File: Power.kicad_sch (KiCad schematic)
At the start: 21 parts, among them U1 HT75xx-1-SOT89, U2 TLV62569DBV, U3 MCP6001-OT

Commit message: Adding official files from course download
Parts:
- removed C1, C2: 1u, symbol Device:C
- removed C3, C4, C5, C6, C9: 22u, symbol Device:C
- removed C7: DNP, symbol Device:C
- removed C8: 100n, symbol Device:C
- removed D1: GREEN, symbol Device:LED
- removed L1: 10n, symbol Device:L
- removed L2: 68u, symbol Device:L
- removed R1: 10R, symbol Device:R_US
- removed R2: 100k, symbol Device:R_US
- removed R3: 22k, symbol Device:R_US
- removed R4, R5, R6: 1k, symbol Device:R_US
- removed U1: HT75xx-1-SOT89, Package_TO_SOT_SMD:SOT-89-3, symbol Regulator_Linear:HT75xx-1-SOT89
- removed U2: TLV62569DBV, Package_TO_SOT_SMD:SOT-23-5, symbol Regulator_Switching:TLV62569DBV
- removed U3: MCP6001-OT, Package_TO_SOT_SMD:SOT-23-5, symbol Amplifier_Operational:MCP6001-OT
- added C100, C101: 1u, Capacitor_SMD:C_0603_1608Metric, symbol Device:C
- added C102, C103, C104, C105, C107: 22u, Capacitor_SMD:C_0805_2012Metric, symbol Device:C
- added C106: DNP, Capacitor_SMD:C_0402_1005Metric, symbol Device:C
- added C108: 100n, Capacitor_SMD:C_0402_1005Metric, symbol Device:C
- added D100: GREEN, LED_SMD:LED_0603_1608Metric, symbol Device:LED
- added L100: 10n, Inductor_SMD:L_0402_1005Metric, symbol Device:L
- added L101: 15u, PhilsLab_Footprints_KiCad6:MWSA0603S, symbol Device:L
- added R100: 10R, Resistor_SMD:R_0805_2012Metric, symbol Device:R
- added R101: 100k, Resistor_SMD:R_0402_1005Metric, symbol Device:R
- added R102: 22k, Resistor_SMD:R_0402_1005Metric, symbol Device:R
- added R103, R104, R105: 1k, Resistor_SMD:R_0402_1005Metric, symbol Device:R
- added U100: HT7533-1, Package_TO_SOT_SMD:SOT-89-3, symbol Regulator_Linear:HT75xx-1-SOT89
- added U101: TLV62569DBV, Package_TO_SOT_SMD:SOT-23-5, symbol Regulator_Switching:TLV62569DBV
- added U102: MCP6001T-E/OT, Package_TO_SOT_SMD:SOT-23-5, symbol Amplifier_Operational:MCP6001-OT
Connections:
- net +3.3VA: now also C103.1, C108.1, R104.2, U100.3 (VOUT), U102.5 (V+)
- net +3V3: now also C105.1, C106.1, D100.2 (A), L101.2, R101.2
- net +5V: now also C101.1, C104.1, L100.2, R100.2, U101.1 (EN), U101.4 (VIN)
- net +5V_FILT: now also C102.1, R100.1, U100.2 (VIN)
- net BUCK_FB: now also C106.2, R101.1, R102.2, U101.5 (FB)
- net GND: now also C100.2, C101.2, C102.2, C103.2, C104.2, C105.2, C107.2, C108.2, R102.1, R103.1, R105.1, U100.1 (GND), U101.2 (GND), U102.2 (V-)
- net LED_PWR_K: now also D100.1 (K), R103.2
- net VBUS: now also C100.1, L100.1
- new net BUCK_SW: L101.1, U101.3 (SW)
- new net VCOM: U102.1, U102.4 (-)
- new net VREF: C107.1, R104.1, R105.2, U102.3 (+)
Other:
- note added: "100mA max."
- note added: "C(in/out)>10uF"
- note added: "DCR=0R15"
- note added: "I(DC)=500mA"
- note added: "I(load)=0.25A max"
- note added: "Input Filtering & Analogue and Digital Supplies"
- note added: "LP filter: fc=15Hz"
- note added: "P(R)>1/8W"
- note added: "V(out)=0.6*(1+100k/22k)=3.327V"
- note added: "VBUS power comes from USB Type C connector (schematic page 2)"
- note added: "WEBENCH Tools"
- note added: "[1] Power"
- note added: "f(sw)=1.5MHz"
- note removed: "100mA max C(in/out) > 10uF"
- note removed: "DCR = OR15 I(DC) = 500mA"
- note removed: "I(load) = 0.25A max f(sw) = 1.5MHz"
- note removed: "Input Filtering & Analog and Digital Supplies"
- note removed: "LP Filter: fc = 15Hz"
- note removed: "P(R) > 1/8W"
- note removed: "Power"
- note removed: "V(out) = 0.6 * (1 + 100k / 22k) = 3.327V"
- note removed: "VBUS power from USB C 2.0 (schematic page 2)"
- company: (none) -> Phil's Lab
- title: (none) -> Mixed-Signal Demo PCB

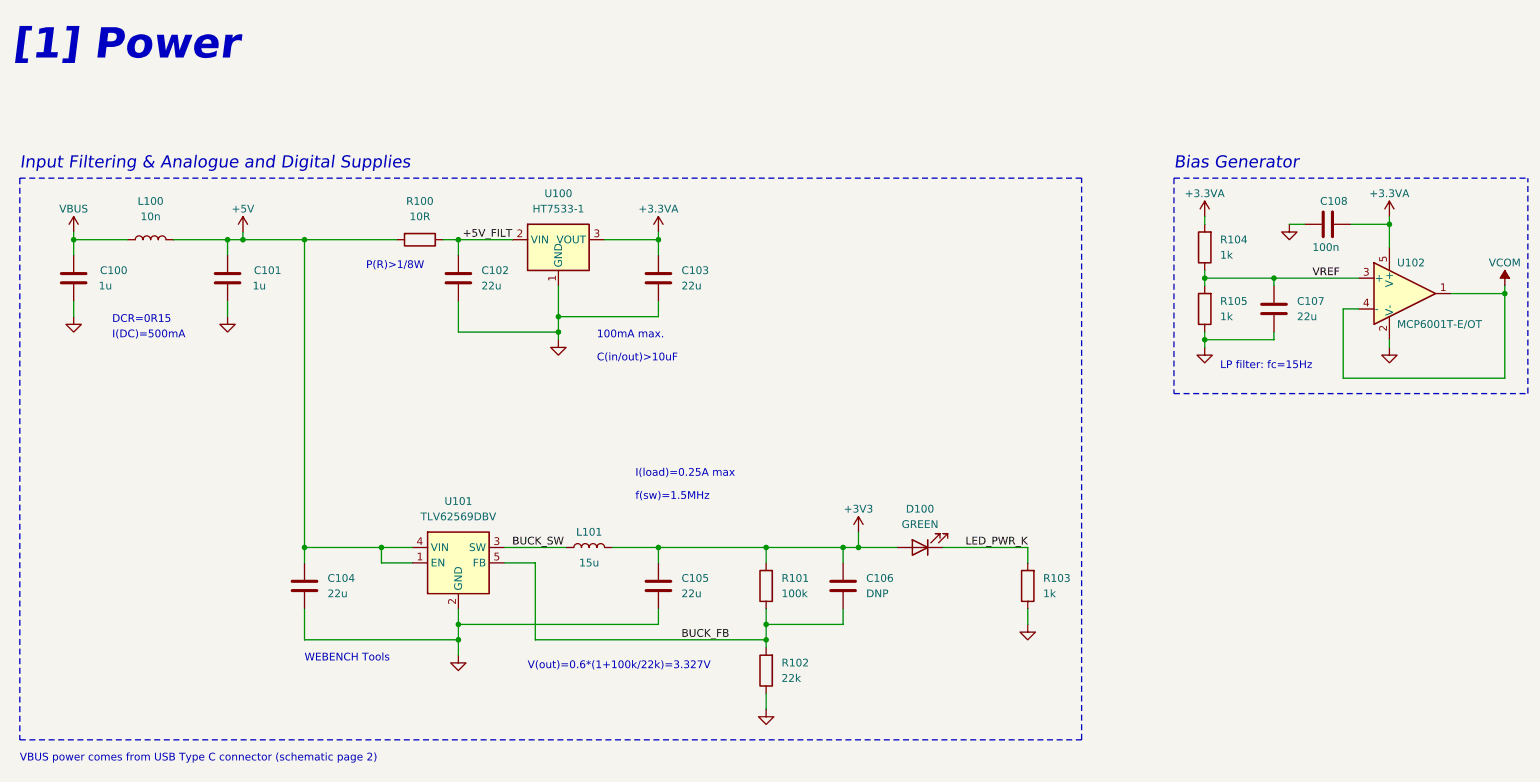
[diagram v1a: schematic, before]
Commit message: Add backup file and updates to schematic
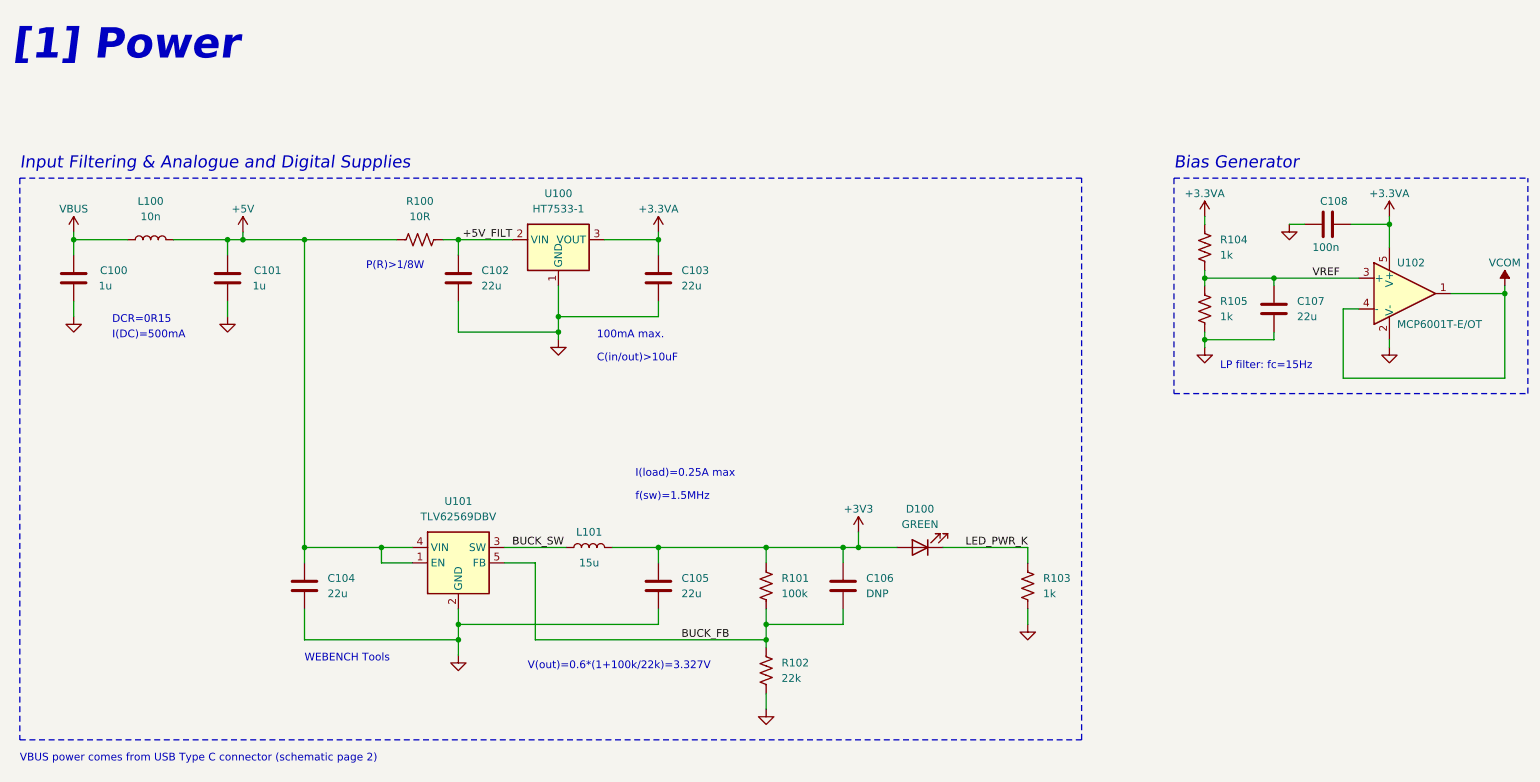
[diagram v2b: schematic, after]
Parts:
- R100, R101, R102, R103, R104, R105: symbol Device:R -> Device:R_US
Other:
- company: Phil's Lab -> Jacob Parent
- title: Mixed-Signal Demo PCB -> Mixed-Signal PCB
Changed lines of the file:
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@@
 	(paper "A4")
 	(title_block
-		(title "Mixed-Signal Demo PCB")
+		(title "Mixed-Signal PCB")
+		(date "6-1-2024")
 		(rev "0.1")
-		(company "Phil's Lab")
+		(company "Jacob Parent")
 	)
 	(junction
@@
 	)
 	(symbol
-		(lib_id "Device:R")
+		(lib_id "Device:R_US")
 		(at 91.44 60.96 270)
 		(unit 1)
@@
 		)
 		(property "Footprint" "Resistor_SMD:R_0805_2012Metric"
-			(at 91.44 59.182 90)
+			(at 91.186 61.976 90)
 			(effects
 				(font
@@
 			)
 		)
-		(property "Description" ""
+		(property "Description" "Resistor, US symbol"
 			(at 91.44 60.96 0)
 			(effects
@@
 	)
 	(symbol
-		(lib_id "Device:R")
+		(lib_id "Device:R_US")
 		(at 220.98 62.23 180)
 		(unit 1)
@@
 		)
 		(property "Footprint" "Resistor_SMD:R_0402_1005Metric"
-			(at 222.758 62.23 90)
+			(at 219.964 61.976 90)
 			(effects
 				(font
@@
 			)
 		)
-		(property "Description" ""
+		(property "Description" "Resistor, US symbol"
 			(at 220.98 62.23 0)
 			(effects
@@
 	)
 	(symbol
-		(lib_id "Device:R")
+		(lib_id "Device:R_US")
 		(at 220.98 72.39 180)
 		(unit 1)
@@
 		)
 		(property "Footprint" "Resistor_SMD:R_0402_1005Metric"
-			(at 222.758 72.39 90)
+			(at 219.964 72.136 90)
 			(effects
 				(font
@@
 			)
 		)
-		(property "Description" ""
+		(property "Description" "Resistor, US symbol"
 			(at 220.98 72.39 0)
 			(effects
@@
 	)
 	(symbol
-		(lib_id "Device:R")
+		(lib_id "Device:R_US")
 		(at 148.59 118.11 180)
 		(unit 1)
@@
 		)
 		(property "Footprint" "Resistor_SMD:R_0402_1005Metric"
-			(at 150.368 118.11 90)
+			(at 147.574 117.856 90)
 			(effects
 				(font
@@
 			)
 		)
-		(property "Description" ""
+		(property "Description" "Resistor, US symbol"
 			(at 148.59 118.11 0)
 			(effects
@@
 	)
 	(symbol
-		(lib_id "Device:R")
+		(lib_id "Device:R_US")
 		(at 148.59 132.08 180)
 		(unit 1)
@@
 		)
 		(property "Footprint" "Resistor_SMD:R_0402_1005Metric"
-			(at 150.368 132.08 90)
+			(at 147.574 131.826 90)
 			(effects
 				(font
@@
 			)
 		)
-		(property "Description" ""
+		(property "Description" "Resistor, US symbol"
 			(at 148.59 132.08 0)
 			(effects
@@
 	)
 	(symbol
-		(lib_id "Device:R")
+		(lib_id "Device:R_US")
 		(at 191.77 118.11 180)
 		(unit 1)
@@
 		)
 		(property "Footprint" "Resistor_SMD:R_0402_1005Metric"
-			(at 193.548 118.11 90)
+			(at 190.754 117.856 90)
 			(effects
 				(font
@@
 			)
 		)
-		(property "Description" ""
+		(property "Description" "Resistor, US symbol"
 			(at 191.77 118.11 0)
 			(effects

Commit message: Add files via upload
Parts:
- L101: footprint PhilsLab_Footprints_KiCad6:MWSA0603S -> Inductor_SMD:L_Sunlord_MWSA0603S
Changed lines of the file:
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@@
 			)
 		)
-		(property "Footprint" "PhilsLab_Footprints_KiCad6:MWSA0603S"
+		(property "Footprint" "Inductor_SMD:L_Sunlord_MWSA0603S"
 			(at 119.38 111.76 0)
 			(effects
